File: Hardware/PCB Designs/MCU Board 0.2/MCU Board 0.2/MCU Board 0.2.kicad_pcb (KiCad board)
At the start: 4 copper layers, 50 x 50 mm, 117 parts, among them CN3 SM04B-SRSS-TB_LF_SN, CN4 SM04B-SRSS-TB_LF_SN, J7 KH-TYPE-C-16P, Q1 MMBT3904, U1 STM32H743VIT6, U2 W25Q128JVS, U4 MAX40200AUK, U5 AP2112K-3.3, U6 ICM-42688-P, U7 MS5611-01BA03-50, U8 USBLC6-2P6, X1 ASDM1-24_000MHZ-LC-T

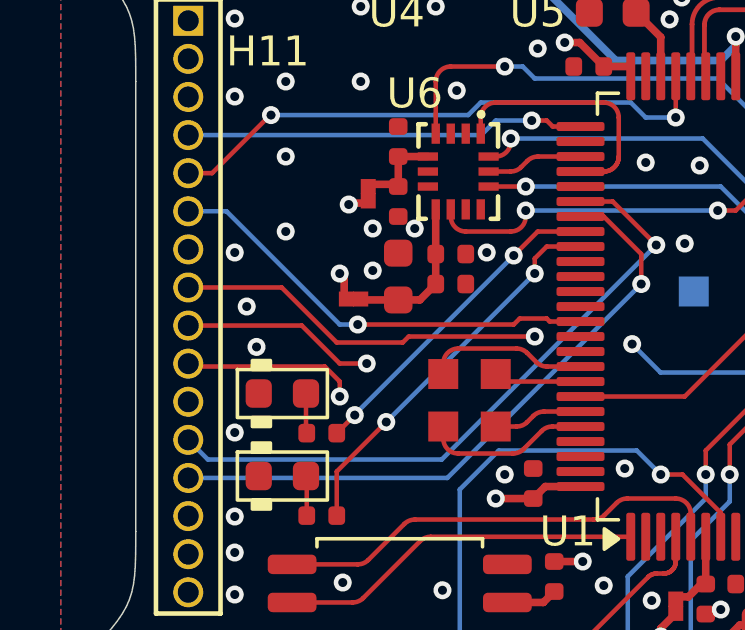
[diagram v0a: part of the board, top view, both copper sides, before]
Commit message: PCB: add rev 0.3 PDB and MCU boards (female BtB sockets on MCU, PWM1 on PB4)
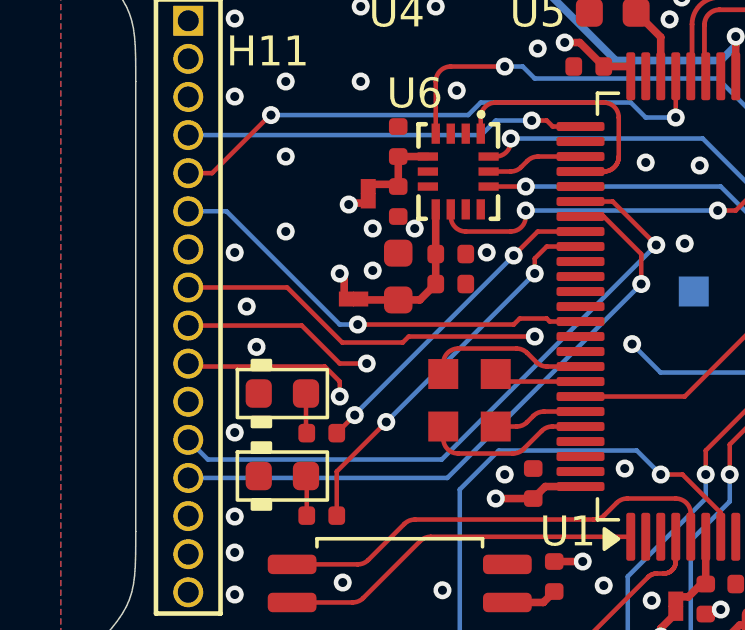
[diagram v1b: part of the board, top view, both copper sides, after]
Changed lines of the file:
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@@
 	)
 	(segment
-		(start 129.2 96.2)
-		(end 131.4 96.2)
+		(start 127.5465 94.365)
+		(end 129.3815 96.2)
 		(width 0.1524)
 		(layer "F.Cu")
@@
 	)
 	(segment
-		(start 124.25 94.365)
-		(end 127.365 94.365)
+		(start 129.3815 96.2)
+		(end 131.4 96.2)
+		(width 0.1524)
+		(layer "F.Cu")
+		(net "PPS")
+	)
+	(segment
+		(start 131.6 96)
+		(end 135.8 96)
 		(width 0.1524)
 		(layer "F.Cu")
@@
 	)
 	(segment
-		(start 131.4 96.2)
-		(end 131.6 96)
+		(start 124.25 94.365)
+		(end 127.5465 94.365)
 		(width 0.1524)
 		(layer "F.Cu")
@@
 	)
 	(segment
-		(start 131.6 96)
-		(end 135.8 96)
+		(start 131.4 96.2)
+		(end 131.6 96)
 		(width 0.1524)
 		(layer "F.Cu")
@@
 		(width 0.1524)
 		(layer "F.Cu")
-		(net "PPS")
-	)
-	(segment
-		(start 127.365 94.365)
-		(end 129.2 96.2)
-		(width 0.1524)
-		(layer "F.Cu")
